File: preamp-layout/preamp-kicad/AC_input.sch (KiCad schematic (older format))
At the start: 7 parts, among them J1 Conn_01x02_Female, J2 Screw_Terminal_01x02, J3 Screw_Terminal_01x02, J4 Screw_Terminal_01x02

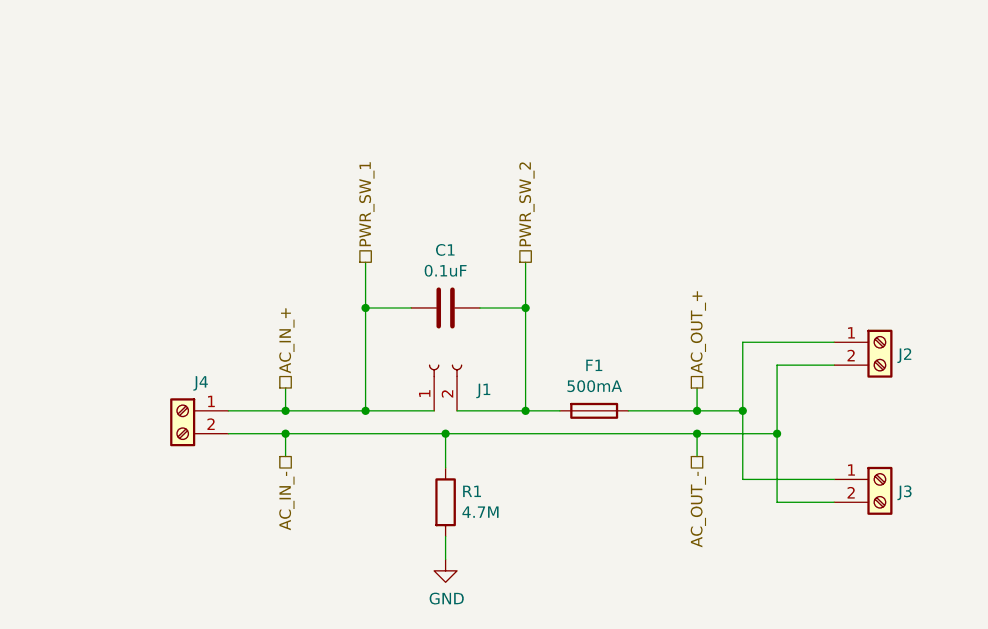
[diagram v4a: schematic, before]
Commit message: Transformer specification
updated schematic, BOM with power transformer info. Other minor schematic tweaks.
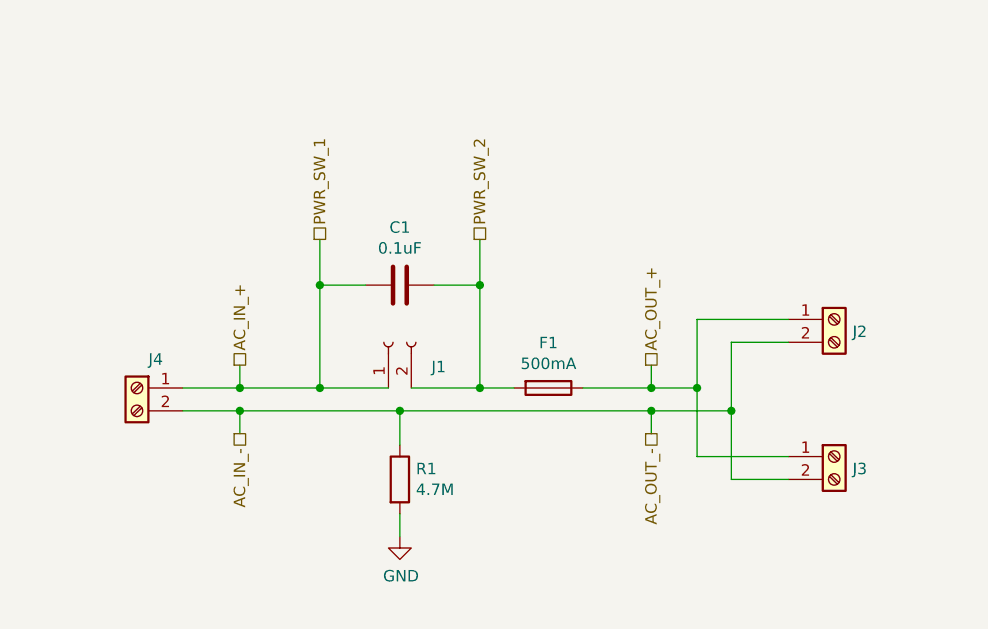
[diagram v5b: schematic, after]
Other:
- moved on the sheet: C1, F1, J1, J2, J3, J4, R1
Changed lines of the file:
@@
 L Device:C C1
 U 1 1 5E2C2703
-P 5650 3500
-F 0 "C1" V 5398 3500 50  0000 C CNN
-F 1 "0.1uF" V 5489 3500 50  0000 C CNN
-F 2 "" H 5688 3350 50  0001 C CNN
-F 3 "~" H 5650 3500 50  0001 C CNN
-	1    5650 3500
+P 5450 3400
+F 0 "C1" V 5198 3400 50  0000 C CNN
+F 1 "0.1uF" V 5289 3400 50  0000 C CNN
+F 2 "" H 5488 3250 50  0001 C CNN
+F 3 "~" H 5450 3400 50  0001 C CNN
+	1    5450 3400
 	0    1    1    0
 $EndComp
 Wire Wire Line
-	5300 3950 5300 3500
+	5100 3850 5100 3400
 Wire Wire Line
-	5300 3500 5500 3500
+	5100 3400 5300 3400
 Wire Wire Line
-	6000 3950 6000 3500
+	5800 3850 5800 3400
 Wire Wire Line
-	6000 3500 5800 3500
+	5800 3400 5600 3400
 $Comp
 L Device:Fuse F1
 U 1 1 5F91375A
-P 6300 3950
-F 0 "F1" V 6103 3950 50  0000 C CNN
-F 1 "500mA" V 6194 3950 50  0000 C CNN
-F 2 "" V 6230 3950 50  0001 C CNN
-F 3 "~" H 6300 3950 50  0001 C CNN
-	1    6300 3950
+P 6100 3850
+F 0 "F1" V 5903 3850 50  0000 C CNN
+F 1 "500mA" V 5994 3850 50  0000 C CNN
+F 2 "" V 6030 3850 50  0001 C CNN
+F 3 "~" H 6100 3850 50  0001 C CNN
+	1    6100 3850
 	0    1    1    0
 $EndComp
 Wire Wire Line
-	6150 3950 6000 3950
-Connection ~ 6000 3950
-Text HLabel 6750 3850 1    50   UnSpc ~ 0
+	5950 3850 5800 3850
+Connection ~ 5800 3850
+Text HLabel 6550 3750 1    50   UnSpc ~ 0
 AC_OUT_+
-Text HLabel 6750 4150 3    50   UnSpc ~ 0
+Text HLabel 6550 4050 3    50   UnSpc ~ 0
 AC_OUT_-
 Wire Wire Line
-	5650 4200 5650 4050
+	5450 4100 5450 3950
 $Comp
 L Device:R R1
 U 1 1 5E2C3357
-P 5650 4350
-F 0 "R1" H 5720 4396 50  0000 L CNN
-F 1 "4.7M" H 5720 4305 50  0000 L CNN
-F 2 "Resistor_THT:R_Axial_DIN0207_L6.3mm_D2.5mm_P10.16mm_Horizontal" V 5580 4350 50  0001 C CNN
-F 3 "~" H 5650 4350 50  0001 C CNN
-	1    5650 4350
+P 5450 4250
+F 0 "R1" H 5520 4296 50  0000 L CNN
+F 1 "4.7M" H 5520 4205 50  0000 L CNN
+F 2 "Resistor_THT:R_Axial_DIN0207_L6.3mm_D2.5mm_P10.16mm_Horizontal" V 5380 4250 50  0001 C CNN
+F 3 "~" H 5450 4250 50  0001 C CNN
+	1    5450 4250
 	1    0    0    -1
 $EndComp
 Wire Wire Line
-	4700 4050 4950 4050
-Connection ~ 5650 4050
+	4500 3950 4750 3950
+Connection ~ 5450 3950
 Wire Wire Line
-	5300 3950 4950 3950
-Connection ~ 5300 3950
+	5100 3850 4750 3850
+Connection ~ 5100 3850
 $Comp
 L power:GND #PWR03
 U 1 1 649E3EA1
-P 5650 4600
-F 0 "#PWR03" H 5650 4350 50  0001 C CNN
-F 1 "GND" H 5655 4427 50  0000 C CNN
-F 2 "" H 5650 4600 50  0001 C CNN
-F 3 "" H 5650 4600 50  0001 C CNN
-	1    5650 4600
+P 5450 4500
+F 0 "#PWR03" H 5450 4250 50  0001 C CNN
+F 1 "GND" H 5455 4327 50  0000 C CNN
+F 2 "" H 5450 4500 50  0001 C CNN
+F 3 "" H 5450 4500 50  0001 C CNN
+	1    5450 4500
 	1    0    0    -1
 $EndComp
@@
 L Connector:Screw_Terminal_01x02 J?
 U 1 1 65B060F9
-P 7550 3650
+P 7350 3550
 AR Path="/5E27B612/65B060F9" Ref="J?"  Part="1"
 AR Path="/5E26F6FE/65B060F9" Ref="J2"  Part="1"
-F 0 "J2" H 7630 3596 50  0000 L CNN
-F 1 "Screw_Terminal_01x02" H 7630 3551 50  0001 L CNN
-F 2 "TerminalBlock_Phoenix:TerminalBlock_Phoenix_PT-1,5-2-5.0-H_1x02_P5.00mm_Horizontal" H 7550 3650 50  0001 C CNN
-F 3 "~" H 7550 3650 50  0001 C CNN
-	1    7550 3650
+F 0 "J2" H 7430 3496 50  0000 L CNN
+F 1 "Screw_Terminal_01x02" H 7430 3451 50  0001 L CNN
+F 2 "TerminalBlock_Phoenix:TerminalBlock_Phoenix_PT-1,5-2-5.0-H_1x02_P5.00mm_Horizontal" H 7350 3550 50  0001 C CNN
+F 3 "~" H 7350 3550 50  0001 C CNN
+	1    7350 3550
 	1    0    0    -1
 $EndComp
@@
 L Connector:Screw_Terminal_01x02 J?
 U 1 1 65B0680E
-P 7550 4250
+P 7350 4150
 AR Path="/5E27B612/65B0680E" Ref="J?"  Part="1"
 AR Path="/5E26F6FE/65B0680E" Ref="J3"  Part="1"
-F 0 "J3" H 7630 4196 50  0000 L CNN
-F 1 "Screw_Terminal_01x02" H 7630 4151 50  0001 L CNN
-F 2 "TerminalBlock_Phoenix:TerminalBlock_Phoenix_PT-1,5-2-5.0-H_1x02_P5.00mm_Horizontal" H 7550 4250 50  0001 C CNN
-F 3 "~" H 7550 4250 50  0001 C CNN
-	1    7550 4250
+F 0 "J3" H 7430 4096 50  0000 L CNN
+F 1 "Screw_Terminal_01x02" H 7430 4051 50  0001 L CNN
+F 2 "TerminalBlock_Phoenix:TerminalBlock_Phoenix_PT-1,5-2-5.0-H_1x02_P5.00mm_Horizontal" H 7350 4150 50  0001 C CNN
+F 3 "~" H 7350 4150 50  0001 C CNN
+	1    7350 4150
 	1    0    0    -1
 $EndComp
@@
 L Connector:Conn_01x02_Female J1
 U 1 1 5E2B212C
-P 5600 3750
-F 0 "J1" V 5492 3562 50  0000 R CNN
-F 1 "Conn_01x02_Female" V 5447 3562 50  0001 R CNN
-F 2 "Connector_JST:JST_EH_B2B-EH-A_1x02_P2.50mm_Vertical" H 5600 3750 50  0001 C CNN
-F 3 "~" H 5600 3750 50  0001 C CNN
-	1    5600 3750
+P 5400 3650
+F 0 "J1" V 5292 3462 50  0000 R CNN
+F 1 "Conn_01x02_Female" V 5247 3462 50  0001 R CNN
+F 2 "Connector_JST:JST_EH_B2B-EH-A_1x02_P2.50mm_Vertical" H 5400 3650 50  0001 C CNN
+F 3 "~" H 5400 3650 50  0001 C CNN
+	1    5400 3650
 	0    -1   -1   0
 $EndComp
 Wire Wire Line
-	5700 3950 6000 3950
+	5500 3850 5800 3850
 Wire Wire Line
-	5300 3950 5600 3950
+	5100 3850 5400 3850
 Wire Wire Line
-	5650 4500 5650 4600
+	5450 4400 5450 4500
 Wire Wire Line
-	6950 3950 6950 3650
+	6750 3850 6750 3550
 Wire Wire Line
-	6950 3650 7350 3650
+	6750 3550 7150 3550
 Wire Wire Line
-	6450 3950 6750 3950
+	6250 3850 6550 3850
 Wire Wire Line
-	7100 3750 7350 3750
+	6900 3650 7150 3650
 Wire Wire Line
-	5650 4050 6750 4050
+	5450 3950 6550 3950
 Wire Wire Line
-	6750 3850 6750 3950
-Connection ~ 6750 3950
+	6550 3750 6550 3850
+Connection ~ 6550 3850
 Wire Wire Line
-	6750 3950 6950 3950
+	6550 3850 6750 3850
 Wire Wire Line
-	6750 4150 6750 4050
-Connection ~ 6750 4050
+	6550 4050 6550 3950
+Connection ~ 6550 3950
 Wire Wire Line
-	6750 4050 7100 4050
-Text HLabel 5300 3300 1    50   UnSpc ~ 0
+	6550 3950 6900 3950
+Text HLabel 5100 3200 1    50   UnSpc ~ 0
 PWR_SW_1
-Text HLabel 6000 3300 1    50   UnSpc ~ 0
+Text HLabel 5800 3200 1    50   UnSpc ~ 0
 PWR_SW_2
 Wire Wire Line
-	5300 3300 5300 3500
-Connection ~ 5300 3500
+	5100 3200 5100 3400
+Connection ~ 5100 3400
 Wire Wire Line
-	6000 3300 6000 3500
-Connection ~ 6000 3500
-Text HLabel 4950 3850 1    50   UnSpc ~ 0
+	5800 3200 5800 3400
+Connection ~ 5800 3400
+Text HLabel 4750 3750 1    50   UnSpc ~ 0
 AC_IN_+
-Text HLabel 4950 4150 3    50   UnSpc ~ 0
+Text HLabel 4750 4050 3    50   UnSpc ~ 0
 AC_IN_-
 $Comp
 L Connector:Screw_Terminal_01x02 J?
 U 1 1 5E330384
-P 4500 3950
+P 4300 3850
 AR Path="/5E27B612/5E330384" Ref="J?"  Part="1"
 AR Path="/5E26F6FE/5E330384" Ref="J4"  Part="1"
-F 0 "J4" H 4418 4075 50  0000 C CNN
-F 1 "Screw_Terminal_01x02" H 4580 3851 50  0001 L CNN
-F 2 "TerminalBlock_Phoenix:TerminalBlock_Phoenix_PT-1,5-2-5.0-H_1x02_P5.00mm_Horizontal" H 4500 3950 50  0001 C CNN
-F 3 "~" H 4500 3950 50  0001 C CNN
-	1    4500 3950
+F 0 "J4" H 4218 3975 50  0000 C CNN
+F 1 "Screw_Terminal_01x02" H 4380 3751 50  0001 L CNN
+F 2 "TerminalBlock_Phoenix:TerminalBlock_Phoenix_PT-1,5-2-5.0-H_1x02_P5.00mm_Horizontal" H 4300 3850 50  0001 C CNN
+F 3 "~" H 4300 3850 50  0001 C CNN
+	1    4300 3850
 	-1   0    0    -1
 $EndComp
 Wire Wire Line
-	7100 4050 7100 3750
+	6900 3950 6900 3650
 Wire Wire Line
-	6950 3950 6950 4250
+	6750 3850 6750 4150
 Wire Wire Line
-	6950 4250 7350 4250
-Connection ~ 6950 3950
+	6750 4150 7150 4150
+Connection ~ 6750 3850
 Wire Wire Line
-	7100 4050 7100 4350
+	6900 3950 6900 4250
 Wire Wire Line
-	7100 4350 7350 4350
-Connection ~ 7100 4050
+	6900 4250 7150 4250
+Connection ~ 6900 3950
 Wire Wire Line
-	4950 3850 4950 3950
-Connection ~ 4950 3950
+	4750 3750 4750 3850
+Connection ~ 4750 3850
 Wire Wire Line
-	4950 3950 4700 3950
+	4750 3850 4500 3850
 Wire Wire Line
-	4950 4150 4950 4050
-Connection ~ 4950 4050
+	4750 4050 4750 3950
+Connection ~ 4750 3950
 Wire Wire Line
-	4950 4050 5650 4050
+	4750 3950 5450 3950
 $EndSCHEMATC

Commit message: screw terminal update
AC power conn update to implement ground. Moved BOM to html file format for web view, not sure if I like it like this but wanted to try it.
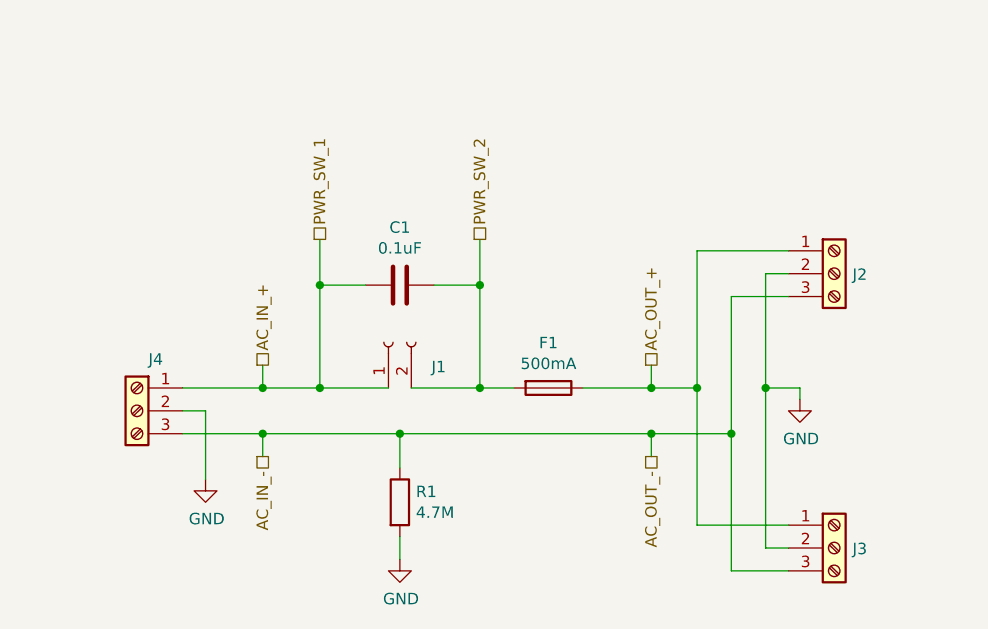
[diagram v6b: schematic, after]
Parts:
- removed J2, J3, J4: Screw_Terminal_01x02, TerminalBlock_Phoenix:TerminalBlock_Phoenix_PT-1,5-2-5.0-H_1x02_P5.00mm_Horizontal, symbol Connector:Screw_Terminal_01x02
- added J2, J3, J4: Screw_Terminal_01x03, TerminalBlock_Phoenix:TerminalBlock_Phoenix_MKDS-3-3-5.08_1x03_P5.08mm_Horizontal, symbol Connector:Screw_Terminal_01x03
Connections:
- net AC_IN_+: now also J4.1 (Pin_1)
- net AC_IN_-: now also J2.3 (Pin_3), J3.3 (Pin_3), J4.3 (Pin_3)
- net AC_OUT_+: now also J2.1 (Pin_1), J3.1 (Pin_1)
- net GND: now also J2.2 (Pin_2), J3.2 (Pin_2), J4.2 (Pin_2)
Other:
- moved on the sheet: R1
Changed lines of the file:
@@
 Text HLabel 6550 3750 1    50   UnSpc ~ 0
 AC_OUT_+
-Text HLabel 6550 4050 3    50   UnSpc ~ 0
+Text HLabel 6550 4150 3    50   UnSpc ~ 0
 AC_OUT_-
 Wire Wire Line
-	5450 4100 5450 3950
+	5450 4200 5450 4050
 $Comp
 L Device:R R1
 U 1 1 5E2C3357
-P 5450 4250
-F 0 "R1" H 5520 4296 50  0000 L CNN
-F 1 "4.7M" H 5520 4205 50  0000 L CNN
-F 2 "Resistor_THT:R_Axial_DIN0207_L6.3mm_D2.5mm_P10.16mm_Horizontal" V 5380 4250 50  0001 C CNN
-F 3 "~" H 5450 4250 50  0001 C CNN
-	1    5450 4250
+P 5450 4350
+F 0 "R1" H 5520 4396 50  0000 L CNN
+F 1 "4.7M" H 5520 4305 50  0000 L CNN
+F 2 "Resistor_THT:R_Axial_DIN0207_L6.3mm_D2.5mm_P10.16mm_Horizontal" V 5380 4350 50  0001 C CNN
+F 3 "~" H 5450 4350 50  0001 C CNN
+	1    5450 4350
 	1    0    0    -1
 $EndComp
-Wire Wire Line
-	4500 3950 4750 3950
-Connection ~ 5450 3950
-Wire Wire Line
-	5100 3850 4750 3850
+Connection ~ 5450 4050
 Connection ~ 5100 3850
 $Comp
 L power:GND #PWR03
 U 1 1 649E3EA1
-P 5450 4500
-F 0 "#PWR03" H 5450 4250 50  0001 C CNN
-F 1 "GND" H 5455 4327 50  0000 C CNN
-F 2 "" H 5450 4500 50  0001 C CNN
-F 3 "" H 5450 4500 50  0001 C CNN
-	1    5450 4500
-	1    0    0    -1
-$EndComp
-$Comp
-L Connector:Screw_Terminal_01x02 J?
-U 1 1 65B060F9
-P 7350 3550
-AR Path="/5E27B612/65B060F9" Ref="J?"  Part="1"
-AR Path="/5E26F6FE/65B060F9" Ref="J2"  Part="1"
-F 0 "J2" H 7430 3496 50  0000 L CNN
-F 1 "Screw_Terminal_01x02" H 7430 3451 50  0001 L CNN
-F 2 "TerminalBlock_Phoenix:TerminalBlock_Phoenix_PT-1,5-2-5.0-H_1x02_P5.00mm_Horizontal" H 7350 3550 50  0001 C CNN
-F 3 "~" H 7350 3550 50  0001 C CNN
-	1    7350 3550
-	1    0    0    -1
-$EndComp
-$Comp
-L Connector:Screw_Terminal_01x02 J?
-U 1 1 65B0680E
-P 7350 4150
-AR Path="/5E27B612/65B0680E" Ref="J?"  Part="1"
-AR Path="/5E26F6FE/65B0680E" Ref="J3"  Part="1"
-F 0 "J3" H 7430 4096 50  0000 L CNN
-F 1 "Screw_Terminal_01x02" H 7430 4051 50  0001 L CNN
-F 2 "TerminalBlock_Phoenix:TerminalBlock_Phoenix_PT-1,5-2-5.0-H_1x02_P5.00mm_Horizontal" H 7350 4150 50  0001 C CNN
-F 3 "~" H 7350 4150 50  0001 C CNN
-	1    7350 4150
+P 5450 4600
+F 0 "#PWR03" H 5450 4350 50  0001 C CNN
+F 1 "GND" H 5455 4427 50  0000 C CNN
+F 2 "" H 5450 4600 50  0001 C CNN
+F 3 "" H 5450 4600 50  0001 C CNN
+	1    5450 4600
 	1    0    0    -1
 $EndComp
@@
 	5100 3850 5400 3850
 Wire Wire Line
-	5450 4400 5450 4500
+	5450 4500 5450 4600
 Wire Wire Line
-	6750 3850 6750 3550
-Wire Wire Line
-	6750 3550 7150 3550
+	6750 3250 7150 3250
 Wire Wire Line
 	6250 3850 6550 3850
 Wire Wire Line
-	6900 3650 7150 3650
+	6900 3450 7150 3450
 Wire Wire Line
-	5450 3950 6550 3950
+	5450 4050 6550 4050
 Wire Wire Line
 	6550 3750 6550 3850
@@
 	6550 3850 6750 3850
 Wire Wire Line
-	6550 4050 6550 3950
-Connection ~ 6550 3950
+	6550 4150 6550 4050
+Connection ~ 6550 4050
 Wire Wire Line
-	6550 3950 6900 3950
+	6550 4050 6900 4050
 Text HLabel 5100 3200 1    50   UnSpc ~ 0
 PWR_SW_1
@@
 	5800 3200 5800 3400
 Connection ~ 5800 3400
-Text HLabel 4750 3750 1    50   UnSpc ~ 0
+Text HLabel 4850 3750 1    50   UnSpc ~ 0
 AC_IN_+
-Text HLabel 4750 4050 3    50   UnSpc ~ 0
+Text HLabel 4850 4150 3    50   UnSpc ~ 0
 AC_IN_-
+Connection ~ 6750 3850
+Wire Wire Line
+	6900 4650 7150 4650
+Wire Wire Line
+	4850 3750 4850 3850
+Wire Wire Line
+	4850 4150 4850 4050
 $Comp
-L Connector:Screw_Terminal_01x02 J?
-U 1 1 5E330384
-P 4300 3850
-AR Path="/5E27B612/5E330384" Ref="J?"  Part="1"
-AR Path="/5E26F6FE/5E330384" Ref="J4"  Part="1"
-F 0 "J4" H 4218 3975 50  0000 C CNN
-F 1 "Screw_Terminal_01x02" H 4380 3751 50  0001 L CNN
-F 2 "TerminalBlock_Phoenix:TerminalBlock_Phoenix_PT-1,5-2-5.0-H_1x02_P5.00mm_Horizontal" H 4300 3850 50  0001 C CNN
-F 3 "~" H 4300 3850 50  0001 C CNN
-	1    4300 3850
+L Connector:Screw_Terminal_01x03 J4
+U 1 1 5E8BB7CA
+P 4300 3950
+F 0 "J4" H 4218 4175 50  0000 C CNN
+F 1 "Screw_Terminal_01x03" H 4218 3716 50  0001 C CNN
+F 2 "TerminalBlock_Phoenix:TerminalBlock_Phoenix_MKDS-3-3-5.08_1x03_P5.08mm_Horizontal" H 4300 3950 50  0001 C CNN
+F 3 "~" H 4300 3950 50  0001 C CNN
+	1    4300 3950
 	-1   0    0    -1
 $EndComp
+$Comp
+L Connector:Screw_Terminal_01x03 J2
+U 1 1 5E8BEBC3
+P 7350 3350
+F 0 "J2" H 7430 3346 50  0000 L CNN
+F 1 "Screw_Terminal_01x03" H 7268 3116 50  0001 C CNN
+F 2 "TerminalBlock_Phoenix:TerminalBlock_Phoenix_MKDS-3-3-5.08_1x03_P5.08mm_Horizontal" H 7350 3350 50  0001 C CNN
+F 3 "~" H 7350 3350 50  0001 C CNN
+	1    7350 3350
+	1    0    0    -1
+$EndComp
+$Comp
+L Connector:Screw_Terminal_01x03 J3
+U 1 1 5E8C1BA2
+P 7350 4550
+F 0 "J3" H 7430 4546 50  0000 L CNN
+F 1 "Screw_Terminal_01x03" H 7268 4316 50  0001 C CNN
+F 2 "TerminalBlock_Phoenix:TerminalBlock_Phoenix_MKDS-3-3-5.08_1x03_P5.08mm_Horizontal" H 7350 4550 50  0001 C CNN
+F 3 "~" H 7350 4550 50  0001 C CNN
+	1    7350 4550
+	1    0    0    -1
+$EndComp
 Wire Wire Line
-	6900 3950 6900 3650
+	7150 3350 7050 3350
 Wire Wire Line
-	6750 3850 6750 4150
+	7050 4550 7150 4550
+$Comp
+L power:GND #PWR?
+U 1 1 5E8C517A
+P 7200 3900
+F 0 "#PWR?" H 7200 3650 50  0001 C CNN
+F 1 "GND" H 7205 3727 50  0000 C CNN
+F 2 "" H 7200 3900 50  0001 C CNN
+F 3 "" H 7200 3900 50  0001 C CNN
+	1    7200 3900
+	1    0    0    -1
+$EndComp
 Wire Wire Line
-	6750 4150 7150 4150
-Connection ~ 6750 3850
+	7200 3900 7200 3850
 Wire Wire Line
-	6900 3950 6900 4250
+	7200 3850 7050 3850
+Connection ~ 7050 3850
 Wire Wire Line
-	6900 4250 7150 4250
-Connection ~ 6900 3950
+	6750 3250 6750 3850
 Wire Wire Line
-	4750 3750 4750 3850
-Connection ~ 4750 3850
+	6900 3450 6900 4050
 Wire Wire Line
-	4750 3850 4500 3850
+	7050 3350 7050 3850
 Wire Wire Line
-	4750 4050 4750 3950
-Connection ~ 4750 3950
+	6750 4450 7150 4450
 Wire Wire Line
-	4750 3950 5450 3950
+	6900 4050 6900 4650
+Connection ~ 6900 4050
+Wire Wire Line
+	6750 3850 6750 4450
+Wire Wire Line
+	7050 3850 7050 4550
+Wire Wire Line
+	4500 4050 4850 4050
+Wire Wire Line
+	4500 3850 4850 3850
+$Comp
+L power:GND #PWR?
+U 1 1 5E8D595F
+P 4600 4250
+F 0 "#PWR?" H 4600 4000 50  0001 C CNN
+F 1 "GND" H 4605 4077 50  0000 C CNN
+F 2 "" H 4600 4250 50  0001 C CNN
+F 3 "" H 4600 4250 50  0001 C CNN
+	1    4600 4250
+	1    0    0    -1
+$EndComp
+Wire Wire Line
+	4500 3950 4600 3950
+Wire Wire Line
+	4600 3950 4600 4250
+Connection ~ 4850 4050
+Wire Wire Line
+	4850 4050 5450 4050
+Connection ~ 4850 3850
+Wire Wire Line
+	4850 3850 5100 3850
 $EndSCHEMATC
